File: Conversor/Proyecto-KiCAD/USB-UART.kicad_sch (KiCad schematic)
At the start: 30 parts, among them P12 USB-B, Q5 IRF7425, SW5 Switch, U15 FT232BL, U16 LP2985-3.3, Y1 6 MHz

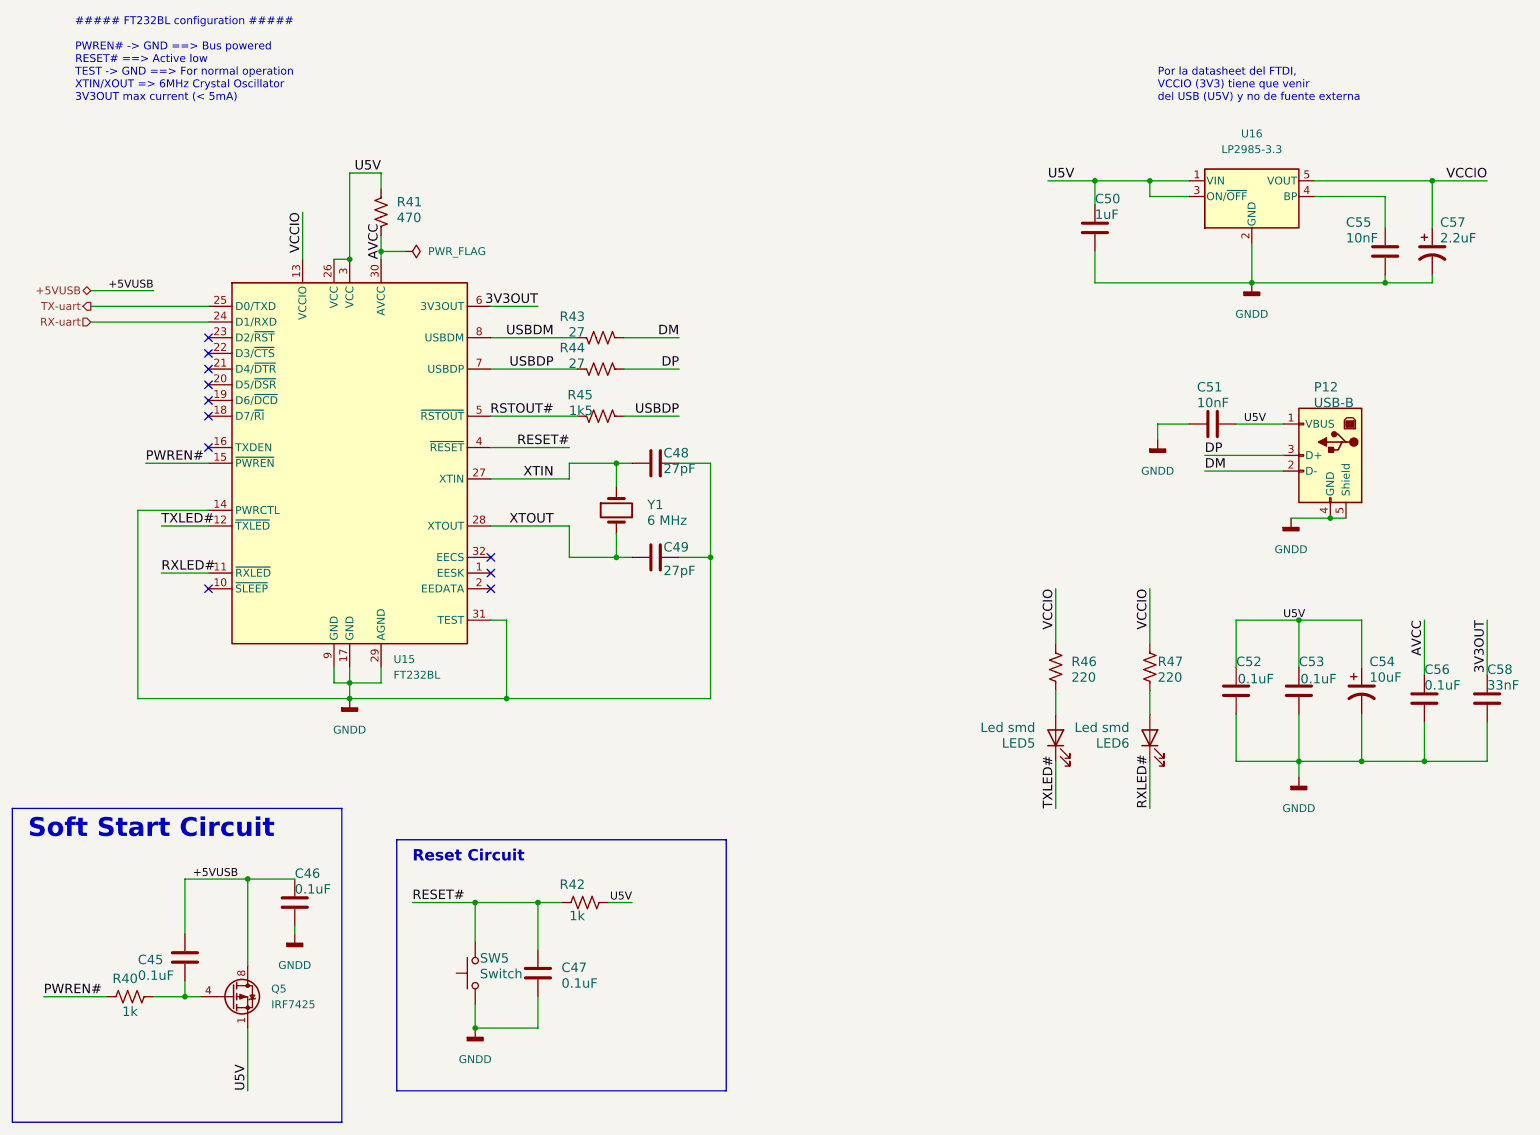
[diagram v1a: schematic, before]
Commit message: Terminar el resto de los cambios de Jorge
- Capacitores electroliticos para el circuito de bootstrap, en paralelo
a los cerámicos
- Cambiar el I2C a 3V3 del lado digital
- Hacer la separacion de linea de datos de I2C del lado digital como en
la nota de aplicación SLYT403A
- Dejar el Vaux del LM5056A con un jumper por si acaso
- Lo mismo con la resistencia de dead-time RDT de los drivers, dejar una
footprint de resistencia SMD para poder cambiarlas de ser necesario
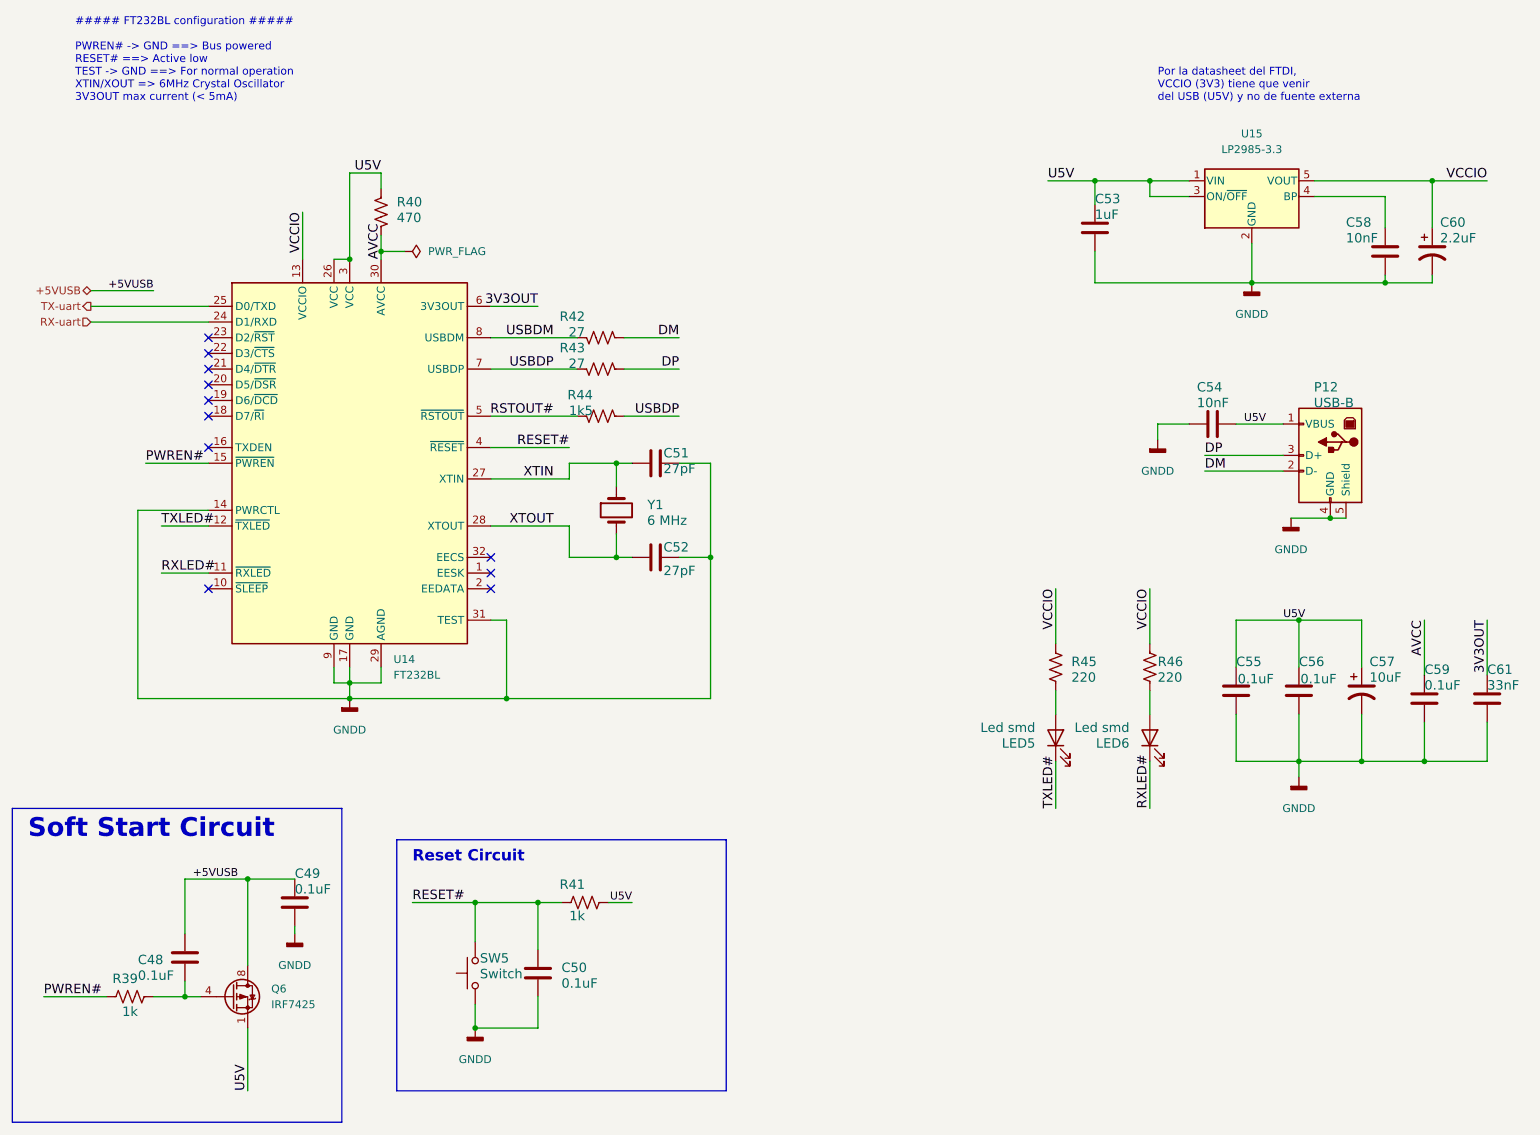
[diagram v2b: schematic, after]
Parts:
- renumbered C45 to C48, C46 to C49, C47 to C50, C48 to C51, C49 to C52, C50 to C53, C51 to C54, C52 to C55, C53 to C56, C54 to C57, C55 to C58, C56 to C59, C57 to C60, C58 to C61, Q5 to Q6, R40 to R39, R41 to R40, R42 to R41, R43 to R42, R44 to R43, R45 to R44, R46 to R45, R47 to R46, U15 to U14, U16 to U15
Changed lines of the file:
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@@
   (symbol (lib_id "Device:C") (at 123.19 87.63 90) (mirror x) (unit 1)
     (in_bom yes) (on_board yes)
-    (property "Reference" "C48" (id 0) (at 124.46 85.09 90)
+    (property "Reference" "C51" (id 0) (at 124.46 85.09 90)
       (effects (font (size 1.524 1.524)) (justify right top))
     )
@@
   (symbol (lib_id "power:GNDD") (at 226.06 96.52 0) (unit 1)
     (in_bom yes) (on_board yes) (fields_autoplaced)
-    (property "Reference" "#PWR098" (id 0) (at 226.06 102.87 0)
+    (property "Reference" "#PWR090" (id 0) (at 226.06 102.87 0)
       (effects (font (size 1.27 1.27)) hide)
     )
@@
   (symbol (lib_id "Device:R_US") (at 114.3 67.31 270) (mirror x) (unit 1)
     (in_bom yes) (on_board yes)
-    (property "Reference" "R43" (id 0) (at 111.76 64.77 90)
+    (property "Reference" "R42" (id 0) (at 111.76 64.77 90)
       (effects (font (size 1.524 1.524)) (justify right top))
     )
@@
   (symbol (lib_id "power:GNDD") (at 204.47 83.82 0) (unit 1)
     (in_bom yes) (on_board yes) (fields_autoplaced)
-    (property "Reference" "#PWR096" (id 0) (at 204.47 90.17 0)
+    (property "Reference" "#PWR088" (id 0) (at 204.47 90.17 0)
       (effects (font (size 1.27 1.27)) hide)
     )
@@
   (symbol (lib_id "power:GNDD") (at 219.71 58.42 0) (unit 1)
     (in_bom yes) (on_board yes) (fields_autoplaced)
-    (property "Reference" "#PWR097" (id 0) (at 219.71 64.77 0)
+    (property "Reference" "#PWR089" (id 0) (at 219.71 64.77 0)
       (effects (font (size 1.27 1.27)) hide)
     )
@@
   (symbol (lib_id "Device:C") (at 46.99 167.64 0) (unit 1)
     (in_bom yes) (on_board yes)
-    (property "Reference" "C45" (id 0) (at 39.37 168.91 0)
+    (property "Reference" "C48" (id 0) (at 39.37 168.91 0)
       (effects (font (size 1.524 1.524)) (justify left bottom))
     )
@@
   (symbol (lib_id "Device:R_US") (at 187.96 120.65 0) (unit 1)
     (in_bom yes) (on_board yes)
-    (property "Reference" "R46" (id 0) (at 190.5 120.65 0)
+    (property "Reference" "R45" (id 0) (at 190.5 120.65 0)
       (effects (font (size 1.524 1.524)) (justify left bottom))
     )
@@
   (symbol (lib_id "Device:R_US") (at 203.2 120.65 0) (unit 1)
     (in_bom yes) (on_board yes)
-    (property "Reference" "R47" (id 0) (at 204.47 120.65 0)
+    (property "Reference" "R46" (id 0) (at 204.47 120.65 0)
       (effects (font (size 1.524 1.524)) (justify left bottom))
     )
@@
   (symbol (lib_id "power:GNDD") (at 227.33 138.43 0) (unit 1)
     (in_bom yes) (on_board yes) (fields_autoplaced)
-    (property "Reference" "#PWR099" (id 0) (at 227.33 144.78 0)
+    (property "Reference" "#PWR091" (id 0) (at 227.33 144.78 0)
       (effects (font (size 1.27 1.27)) hide)
     )
@@
   (symbol (lib_id "Device:R_US") (at 114.3 80.01 270) (mirror x) (unit 1)
     (in_bom yes) (on_board yes)
-    (property "Reference" "R45" (id 0) (at 113.03 77.47 90)
+    (property "Reference" "R44" (id 0) (at 113.03 77.47 90)
       (effects (font (size 1.524 1.524)) (justify right top))
     )
@@
   (symbol (lib_id "Device:R_US") (at 78.74 46.99 0) (mirror x) (unit 1)
     (in_bom yes) (on_board yes)
-    (property "Reference" "R41" (id 0) (at 81.28 44.45 0)
+    (property "Reference" "R40" (id 0) (at 81.28 44.45 0)
       (effects (font (size 1.524 1.524)) (justify left bottom))
     )
@@
   (symbol (lib_id "power:GNDD") (at 93.98 179.07 0) (unit 1)
     (in_bom yes) (on_board yes) (fields_autoplaced)
-    (property "Reference" "#PWR095" (id 0) (at 93.98 185.42 0)
+    (property "Reference" "#PWR087" (id 0) (at 93.98 185.42 0)
       (effects (font (size 1.27 1.27)) hide)
     )
@@
   (symbol (lib_id "Device:C") (at 257.81 125.73 180) (unit 1)
     (in_bom yes) (on_board yes)
-    (property "Reference" "C58" (id 0) (at 257.81 121.92 0)
+    (property "Reference" "C61" (id 0) (at 257.81 121.92 0)
       (effects (font (size 1.524 1.524)) (justify right top))
     )
@@
   (symbol (lib_id "Device:R_US") (at 111.76 158.75 90) (unit 1)
     (in_bom yes) (on_board yes)
-    (property "Reference" "R42" (id 0) (at 111.76 154.94 90)
+    (property "Reference" "R41" (id 0) (at 111.76 154.94 90)
       (effects (font (size 1.524 1.524)) (justify left bottom))
     )
@@
   (symbol (lib_id "Device:R_US") (at 38.1 173.99 90) (unit 1)
     (in_bom yes) (on_board yes)
-    (property "Reference" "R40" (id 0) (at 39.37 170.18 90)
+    (property "Reference" "R39" (id 0) (at 39.37 170.18 90)
       (effects (font (size 1.524 1.524)) (justify left bottom))
     )
@@
   (symbol (lib_id "power:GNDD") (at 73.66 125.73 0) (unit 1)
     (in_bom yes) (on_board yes) (fields_autoplaced)
-    (property "Reference" "#PWR094" (id 0) (at 73.66 132.08 0)
+    (property "Reference" "#PWR086" (id 0) (at 73.66 132.08 0)
       (effects (font (size 1.27 1.27)) hide)
     )
@@
   (symbol (lib_id "Regulator_Linear:LP2985-3.3") (at 219.71 44.45 0) (unit 1)
     (in_bom yes) (on_board yes) (fields_autoplaced)
-    (property "Reference" "U16" (id 0) (at 219.71 34.29 0))
+    (property "Reference" "U15" (id 0) (at 219.71 34.29 0))
     (property "Value" "LP2985-3.3" (id 1) (at 219.71 36.83 0))
     (property "Footprint" "Package_TO_SOT_SMD:SOT-23-5" (id 2) (at 219.71 36.195 0)
@@
   (symbol (lib_id "Device:C") (at 194.31 49.53 0) (unit 1)
     (in_bom yes) (on_board yes)
-    (property "Reference" "C50" (id 0) (at 194.31 45.72 0)
+    (property "Reference" "C53" (id 0) (at 194.31 45.72 0)
       (effects (font (size 1.524 1.524)) (justify left bottom))
     )
@@
   (symbol (lib_id "Interface_USB:FT232BM") (at 73.66 87.63 0) (unit 1)
     (in_bom yes) (on_board yes) (fields_autoplaced)
-    (property "Reference" "U15" (id 0) (at 80.7594 119.38 0)
+    (property "Reference" "U14" (id 0) (at 80.7594 119.38 0)
       (effects (font (size 1.27 1.27)) (justify left))
     )
@@
   (symbol (lib_id "Device:C_Polarized_US") (at 237.49 124.46 0) (unit 1)
     (in_bom yes) (on_board yes)
-    (property "Reference" "C54" (id 0) (at 238.76 120.65 0)
+    (property "Reference" "C57" (id 0) (at 238.76 120.65 0)
       (effects (font (size 1.524 1.524)) (justify left bottom))
     )
@@
   (symbol (lib_id "Transistor_FET:IRF7404") (at 54.61 173.99 0) (unit 1)
     (in_bom yes) (on_board yes) (fields_autoplaced)
-    (property "Reference" "Q5" (id 0) (at 60.96 172.7199 0)
+    (property "Reference" "Q6" (id 0) (at 60.96 172.7199 0)
       (effects (font (size 1.27 1.27)) (justify left))
     )
@@
   (symbol (lib_id "Device:C") (at 227.33 124.46 180) (unit 1)
     (in_bom yes) (on_board yes)
-    (property "Reference" "C53" (id 0) (at 227.33 120.65 0)
+    (property "Reference" "C56" (id 0) (at 227.33 120.65 0)
       (effects (font (size 1.524 1.524)) (justify right top))
     )
@@
   (symbol (lib_id "Device:R_US") (at 114.3 72.39 270) (mirror x) (unit 1)
     (in_bom yes) (on_board yes)
-    (property "Reference" "R44" (id 0) (at 111.76 69.85 90)
+    (property "Reference" "R43" (id 0) (at 111.76 69.85 90)
       (effects (font (size 1.524 1.524)) (justify right top))
     )
@@
   (symbol (lib_id "Device:C_Polarized_US") (at 248.92 53.34 0) (unit 1)
     (in_bom yes) (on_board yes)
-    (property "Reference" "C57" (id 0) (at 250.19 49.53 0)
+    (property "Reference" "C60" (id 0) (at 250.19 49.53 0)
       (effects (font (size 1.524 1.524)) (justify left bottom))
     )
@@
   (symbol (lib_id "Device:C") (at 217.17 124.46 180) (unit 1)
     (in_bom yes) (on_board yes)
-    (property "Reference" "C52" (id 0) (at 217.17 120.65 0)
+    (property "Reference" "C55" (id 0) (at 217.17 120.65 0)
       (effects (font (size 1.524 1.524)) (justify right top))
     )
@@
   (symbol (lib_id "power:GNDD") (at 64.77 163.83 0) (unit 1)
     (in_bom yes) (on_board yes) (fields_autoplaced)
-    (property "Reference" "#PWR093" (id 0) (at 64.77 170.18 0)
+    (property "Reference" "#PWR085" (id 0) (at 64.77 170.18 0)
       (effects (font (size 1.27 1.27)) hide)
     )
@@
   (symbol (lib_id "Device:C") (at 241.3 53.34 0) (unit 1)
     (in_bom yes) (on_board yes)
-    (property "Reference" "C55" (id 0) (at 234.95 49.53 0)
+    (property "Reference" "C58" (id 0) (at 234.95 49.53 0)
       (effects (font (size 1.524 1.524)) (justify left bottom))
     )
@@
   (symbol (lib_id "Device:C") (at 123.19 102.87 90) (mirror x) (unit 1)
     (in_bom yes) (on_board yes)
-    (property "Reference" "C49" (id 0) (at 124.46 100.33 90)
+    (property "Reference" "C52" (id 0) (at 124.46 100.33 90)
       (effects (font (size 1.524 1.524)) (justify right top))
     )
@@
   (symbol (lib_id "Device:C") (at 104.14 170.18 0) (unit 1)
     (in_bom yes) (on_board yes)
-    (property "Reference" "C47" (id 0) (at 107.95 170.18 0)
+    (property "Reference" "C50" (id 0) (at 107.95 170.18 0)
       (effects (font (size 1.524 1.524)) (justify left bottom))
     )
@@
   (symbol (lib_id "Device:C") (at 64.77 158.75 0) (unit 1)
     (in_bom yes) (on_board yes)
-    (property "Reference" "C46" (id 0) (at 64.77 154.94 0)
+    (property "Reference" "C49" (id 0) (at 64.77 154.94 0)
       (effects (font (size 1.524 1.524)) (justify left bottom))
     )
@@
   (symbol (lib_id "Device:C") (at 247.65 125.73 180) (unit 1)
     (in_bom yes) (on_board yes)
-    (property "Reference" "C56" (id 0) (at 247.65 121.92 0)
+    (property "Reference" "C59" (id 0) (at 247.65 121.92 0)
       (effects (font (size 1.524 1.524)) (justify right top))
     )
@@
   (symbol (lib_id "Device:C") (at 213.36 81.28 90) (unit 1)
     (in_bom yes) (on_board yes)
-    (property "Reference" "C51" (id 0) (at 210.82 76.2 90)
-      (effects (font (size 1.524 1.524)) (justify right top))
-    )
+    (property "Reference" "C54" (id 0) (at 210.82 76.2 90)
+      (effects (font (size 1.524 1.524)) (justify right top))
+    )
